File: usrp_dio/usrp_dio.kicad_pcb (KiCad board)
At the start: 2 copper layers, 58.4 x 27.9 mm, 8 parts, among them P1 CONN_01X15, P2 CONN_02X08, P3 CONN_02X08, P4 CONN_02X08, P5 CONN_02X08, U1 74HC595

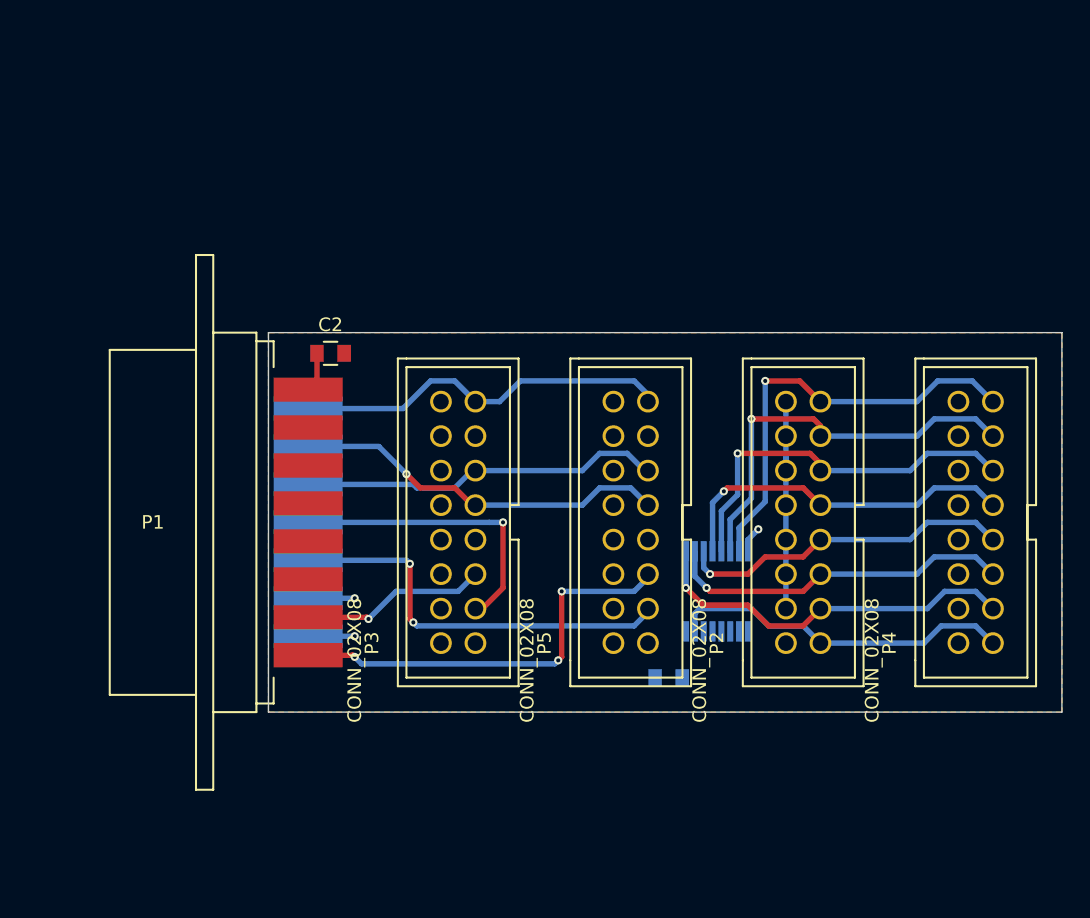
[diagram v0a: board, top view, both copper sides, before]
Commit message: added script to generate ifcfg files for usrp server
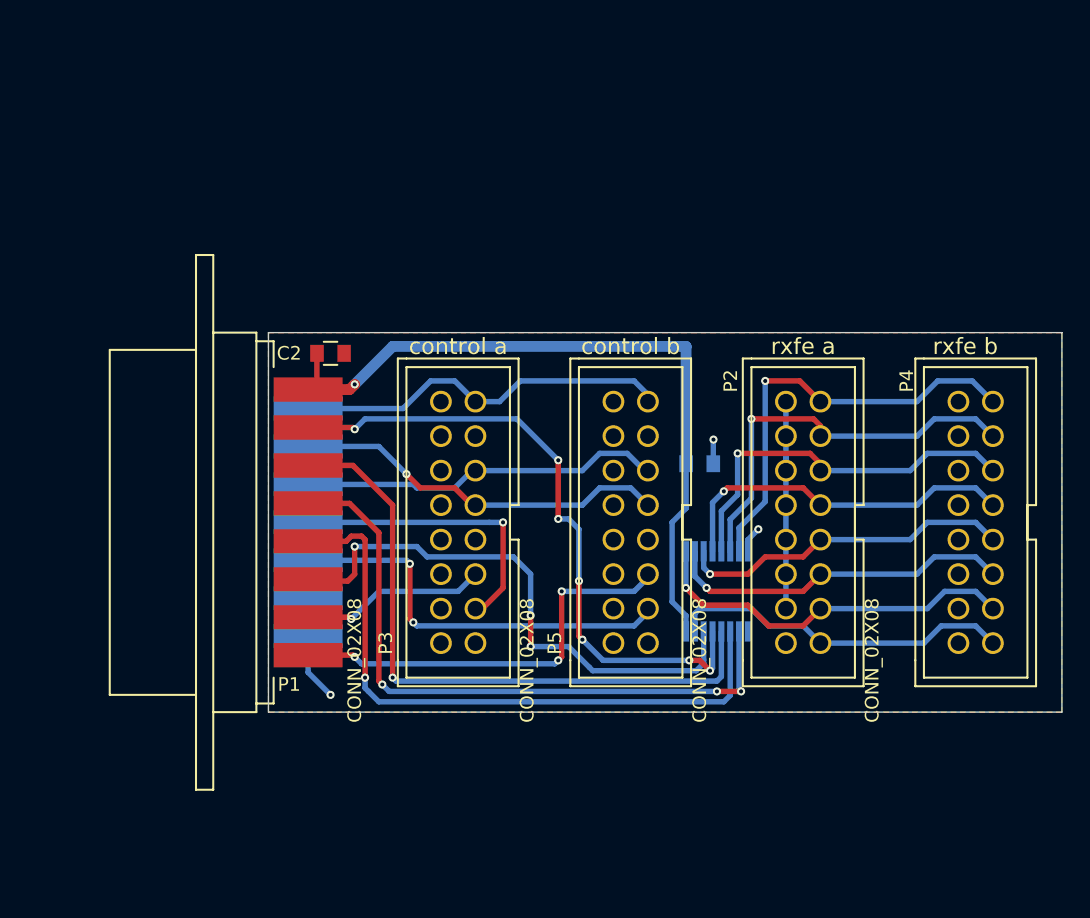
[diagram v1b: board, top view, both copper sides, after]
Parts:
- moved C1 15.9 mm to (154.9, 84.6), turned to 0 degrees
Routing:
- net VCC: track 2.94 -> 53.9 mm, vias 0 -> 1
- net /D2: track 0.00 -> 48.5 mm, vias 0 -> 3
- net /D1: track 0.00 -> 47.9 mm, vias 0 -> 1
- net /D0: track 0.00 -> 47.7 mm, vias 0 -> 7
- net /D3: track 0.00 -> 47.6 mm, vias 0 -> 1
- net /D4: track 0.00 -> 40.9 mm, vias 0 -> 3
- net GND: track 26.1 -> 28.8 mm
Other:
- board text added: "control a"
- board text added: "control b"
- board text added: "rxfe a"
- board text added: "rxfe b"

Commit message: updated usrp dio layout to send more gpio lines to agc boards
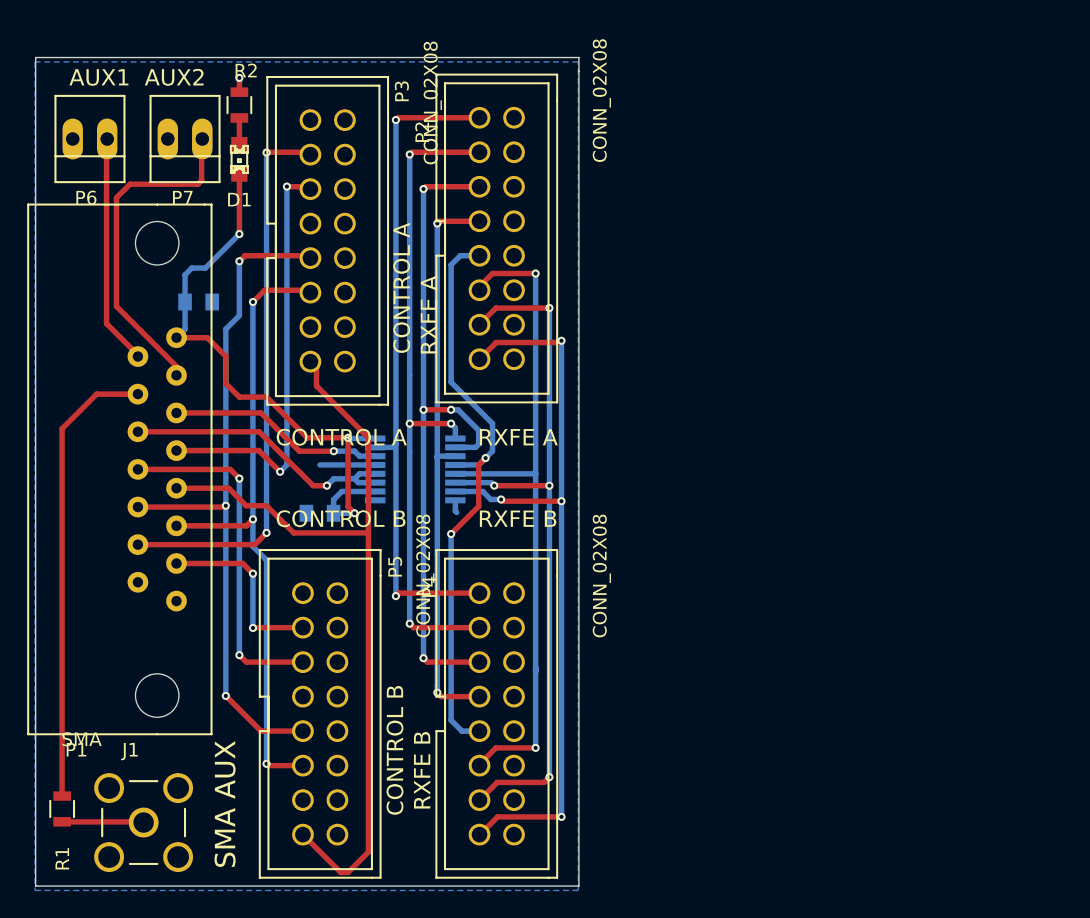
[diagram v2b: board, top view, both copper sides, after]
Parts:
- added D1: LED, LEDs:LED-0805, F.Cu at (121.0, 62.2)
- added J1: SMA, local:SMA_5-1814832-1, F.Cu at (114.0, 111.0)
- added P6: CONN_01X02, Connect:PINHEAD1-2, F.Cu at (110.0, 60.7)
- added P7: CONN_01X02, Connect:PINHEAD1-2, F.Cu at (117.0, 60.7)
- added R1: R, Resistors_SMD:R_0805, F.Cu at (108.0, 110.0)
- added R2: R, Resistors_SMD:R_0805, F.Cu at (121.0, 58.2)
- C2: moved to B.Cu
- P1: footprint Connect:DB15M_CI -> sdtransmitter:182-015-113R531_dsub15
- moved C1 38.8 mm to (118.0, 72.7)
- moved P4 38.0 mm to (140.0, 103.0), turned to 270 degrees
- moved P2 30.8 mm to (140.0, 68.0), turned to 270 degrees
- moved P5 26.9 mm to (127.0, 103.0), turned to 270 degrees
- moved U1 24.0 mm to (134.0, 85.0), turned to 180 degrees
- moved P3 22.8 mm to (127.5, 68.2), turned to 270 degrees
- moved C2 11.8 mm to (127.0, 88.2), turned to 180 degrees
- moved P1 9.30 mm to (115.0, 85.0)
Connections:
- P3 pad 1: Net-(P3-Pad1) -> (no net)
- P3 pad 13: Net-(P3-Pad13) -> (no net)
- P3 pad 7: Net-(P3-Pad7) -> (no net)
- P5 pad 1: Net-(P5-Pad1) -> (no net)
- P5 pad 13: Net-(P5-Pad13) -> (no net)
- P5 pad 7: Net-(P5-Pad7) -> (no net)
- U1 pad 10: /D2 -> VCC
- U1 pad 11: /D3 -> /D4
- U1 pad 12: /D1 -> /D4
- U1 pad 13: /D0 -> GND
- U1 pad 14: /D4 -> /D3
- U1 pad 9: Net-(U1-Pad9) -> (no net)
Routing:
- net /D7: track 28.1 -> 60.0 mm
- net /D3: track 47.6 -> 15.9 mm
- net /D0: track 47.7 -> 18.7 mm, vias 7 -> 0
- net /QC: track 25.8 -> 50.5 mm, vias 1 -> 4
- net /QH: track 32.0 -> 56.3 mm, vias 1 -> 4
- net /D8: track 27.9 -> 51.5 mm, vias 1 -> 3
- net /QA: track 25.5 -> 49.1 mm, vias 0 -> 2
- net /QG: track 30.2 -> 53.1 mm, vias 1 -> 4
- net /QF: track 28.4 -> 51.1 mm, vias 1 -> 2
- net GND: track 28.8 -> 6.06 mm, vias 3 -> 1
- net /D1: track 47.9 -> 25.4 mm, vias 1 -> 0
- net /QB: track 28.0 -> 49.3 mm, vias 1 -> 4
- net /D9: track 27.2 -> 48.0 mm, vias 0 -> 3
- net /D4: track 40.9 -> 21.1 mm, vias 3 -> 1
- net /D10: track 21.8 -> 41.5 mm, vias 1 -> 2
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- added copper zone on B.Cu, net GND
- removed copper zone on F.Cu, net GND
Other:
- board size 58.4 x 27.9 mm -> 40 x 61 mm
- board text added: "AUX1 AUX2"
- board text added: "CONTROL A"
- board text added: "CONTROL B"
- board text added: "RXFE A"
- board text added: "RXFE B"
- board text added: "SMA AUX"
- board text removed: "control a"
- board text removed: "control b"
- board text removed: "rxfe a"
- board text removed: "rxfe b"
